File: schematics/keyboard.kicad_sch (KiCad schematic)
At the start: 33 parts, among them J2 Mini-DIN-6, Q1 2N7000, Q2 2N7000, Q3 2N7000, Q4 2N7000, U18 74HC14, U19 74HC04, U20 74HC00, U21 ATF22V10C-7, U22 74HC280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

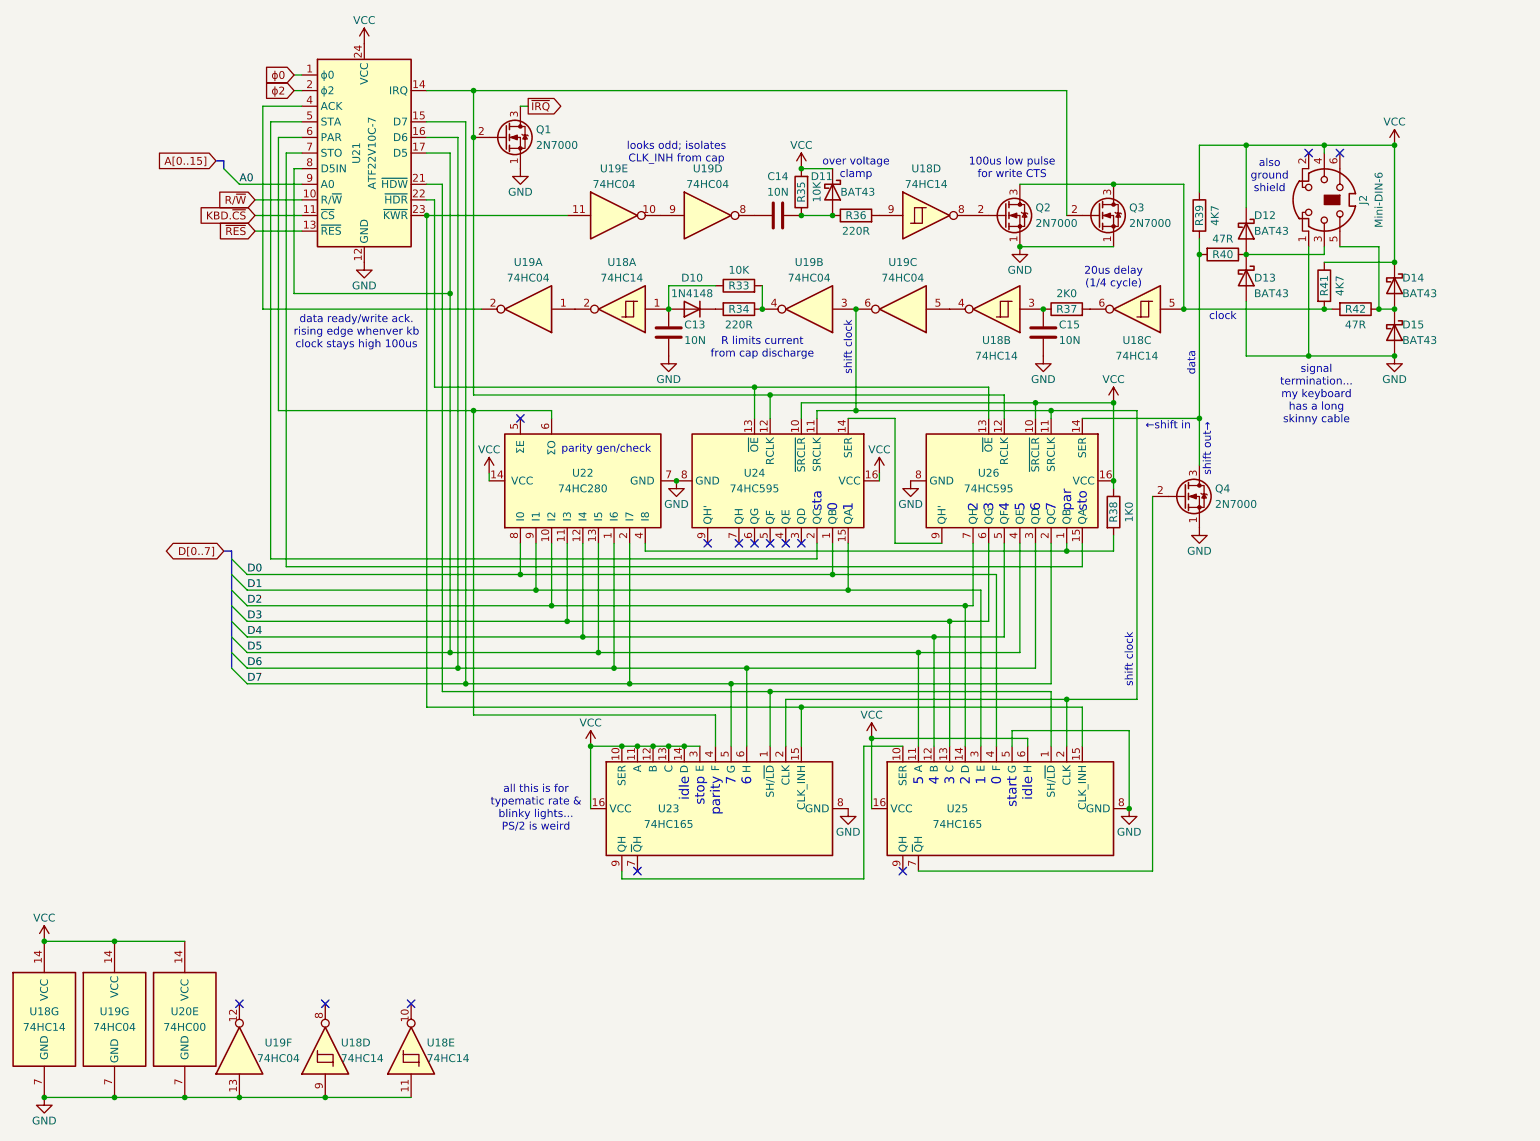
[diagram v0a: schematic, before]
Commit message: combined reset inputs in the pld
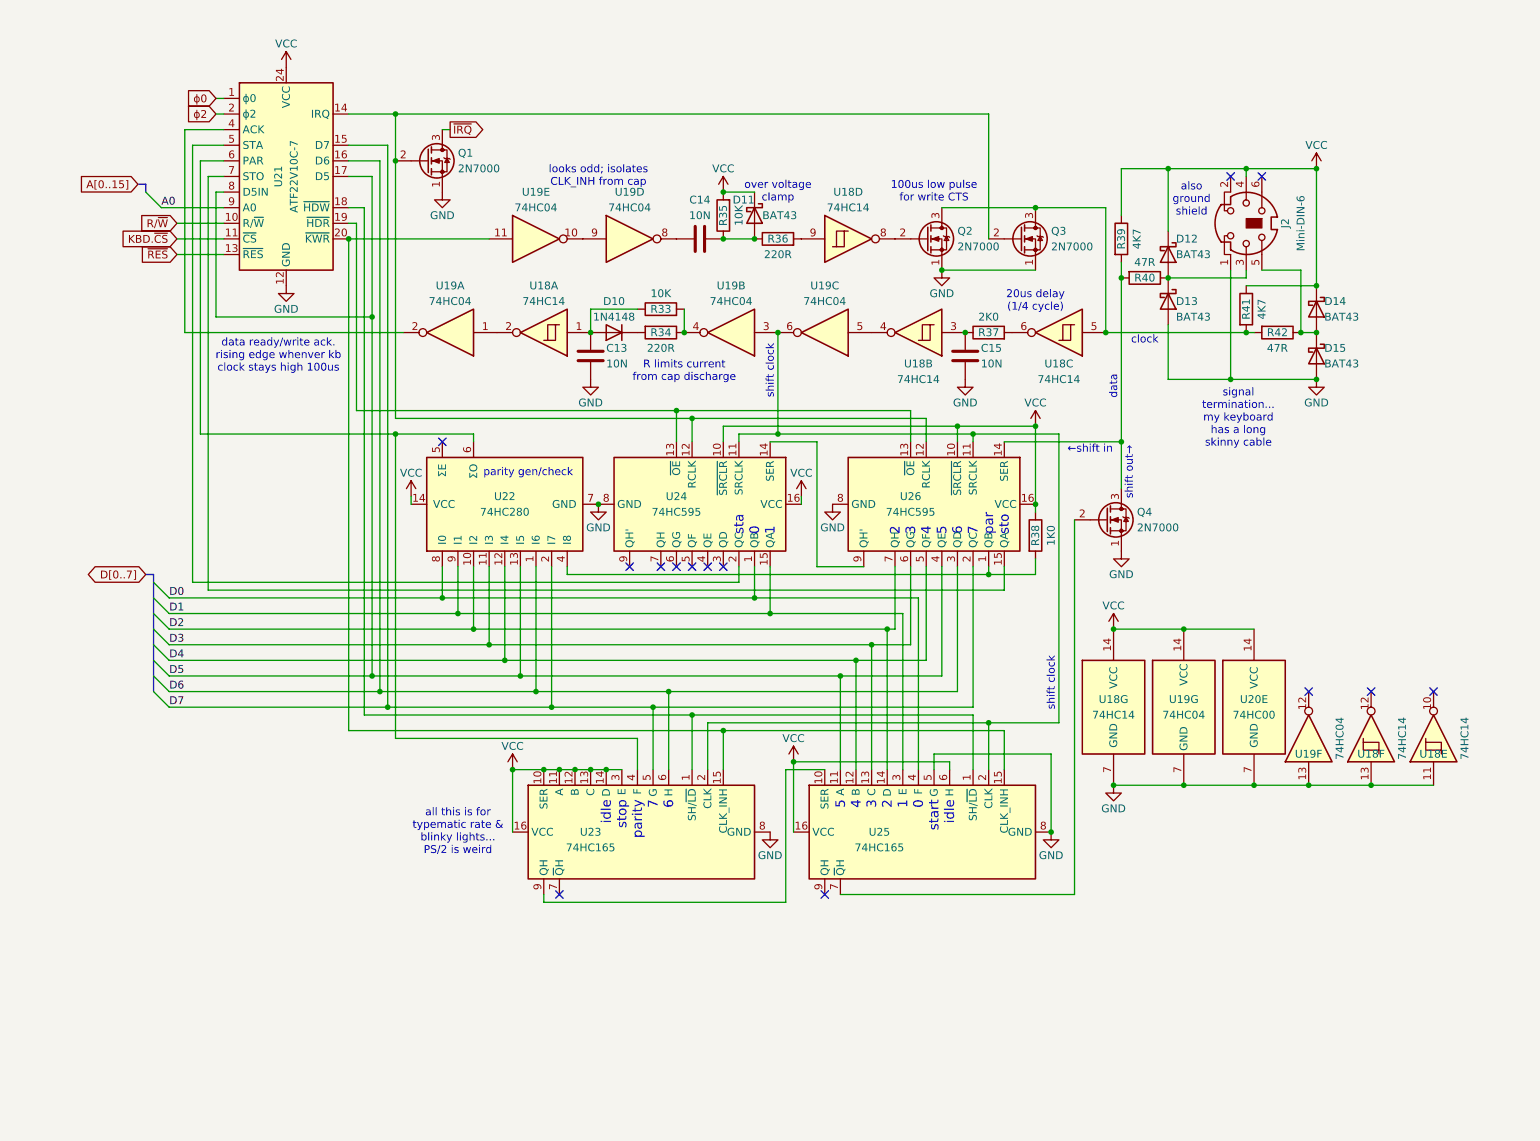
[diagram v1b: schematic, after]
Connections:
- net GND: now also U18.13; no longer U18.9
- net at U24.13 (~{OE}), U26.13 (~{OE}): now also U21.19 (~{HDR}); no longer U21.22 (~{HDR})
- net at U21.18 (~{HDW}): now also U23.1 (SH/~{LD}), U25.1 (SH/~{LD})
- net at U21.20 (~{KWR}): now also U19.11, U23.15 (CLK_INH), U25.15 (CLK_INH)
- now unconnected: U21.21 (~{HDW}), U21.23 (~{KWR})
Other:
- moved on the sheet: C13, C14, C15, D10, D11, D12, D13, D14, D15, J2, Q1, Q2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

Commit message: removed the 74hc04 from the keyboard
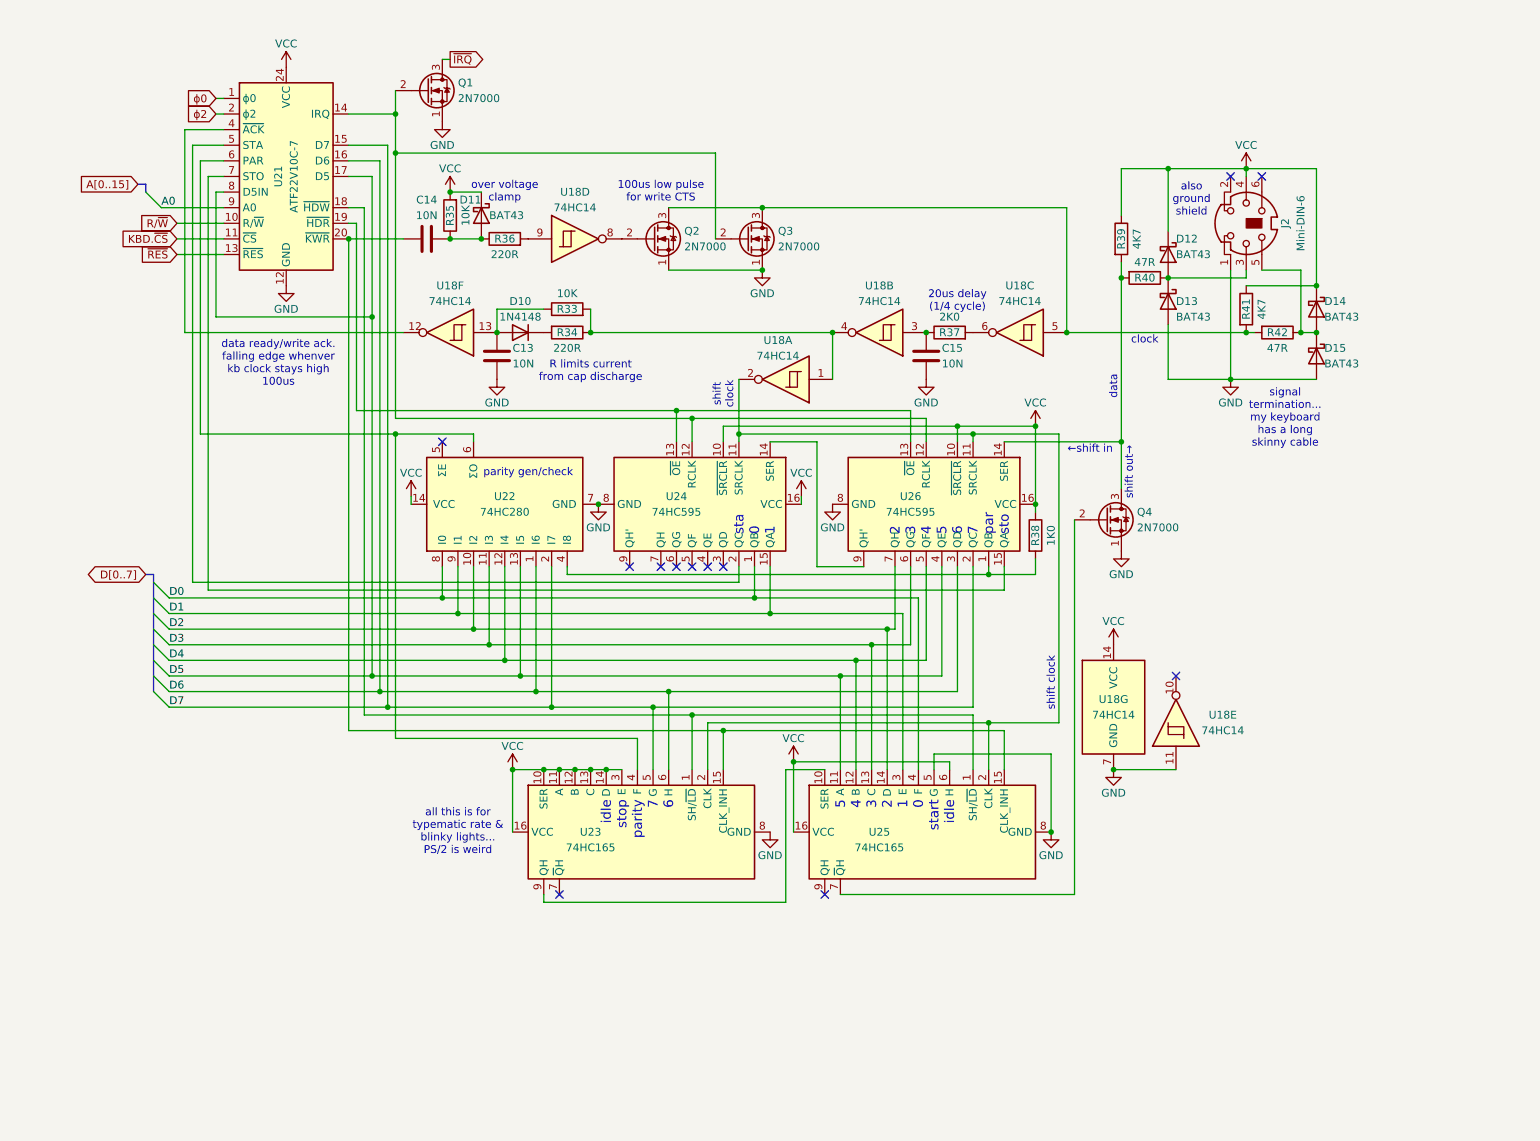
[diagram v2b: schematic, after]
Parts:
- removed unit 6 of U18
- removed U19: 74HC04, symbol 74xx:74HC04
- removed U20: 74HC00, symbol 74xx:74HC00
- added unit 1 of U18
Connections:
- net at U23.2 (CLK), U24.11 (SRCLK), U25.2 (CLK)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: now also U18.2
- net at U21.20 (~{KWR}), U23.15 (CLK_INH), U25.15 (CLK_INH): now also C14.1
- net at U21.4 (~{ACK}): now also U18.12
- net at C13.1, D10.2 (A), R33.1: now also U18.13; no longer U18.1
- net at U18.4: now also R33.2, R34.1, U18.1
- no-connect marks 14 -> 12
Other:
- note added: "data ready/write ack. falling edge whenver kb clock stays high 100us"
- note removed: "data ready/write ack. rising edge whenver kb clock stays high 100us"
- note removed: "looks odd; isolates CLK_INH from cap"
- moved on the sheet: C13, C14, C15, D10, D11, Q1, Q2, Q3, R33, R34, R35, R36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

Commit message: re-added the 74hc04 to the keyboard
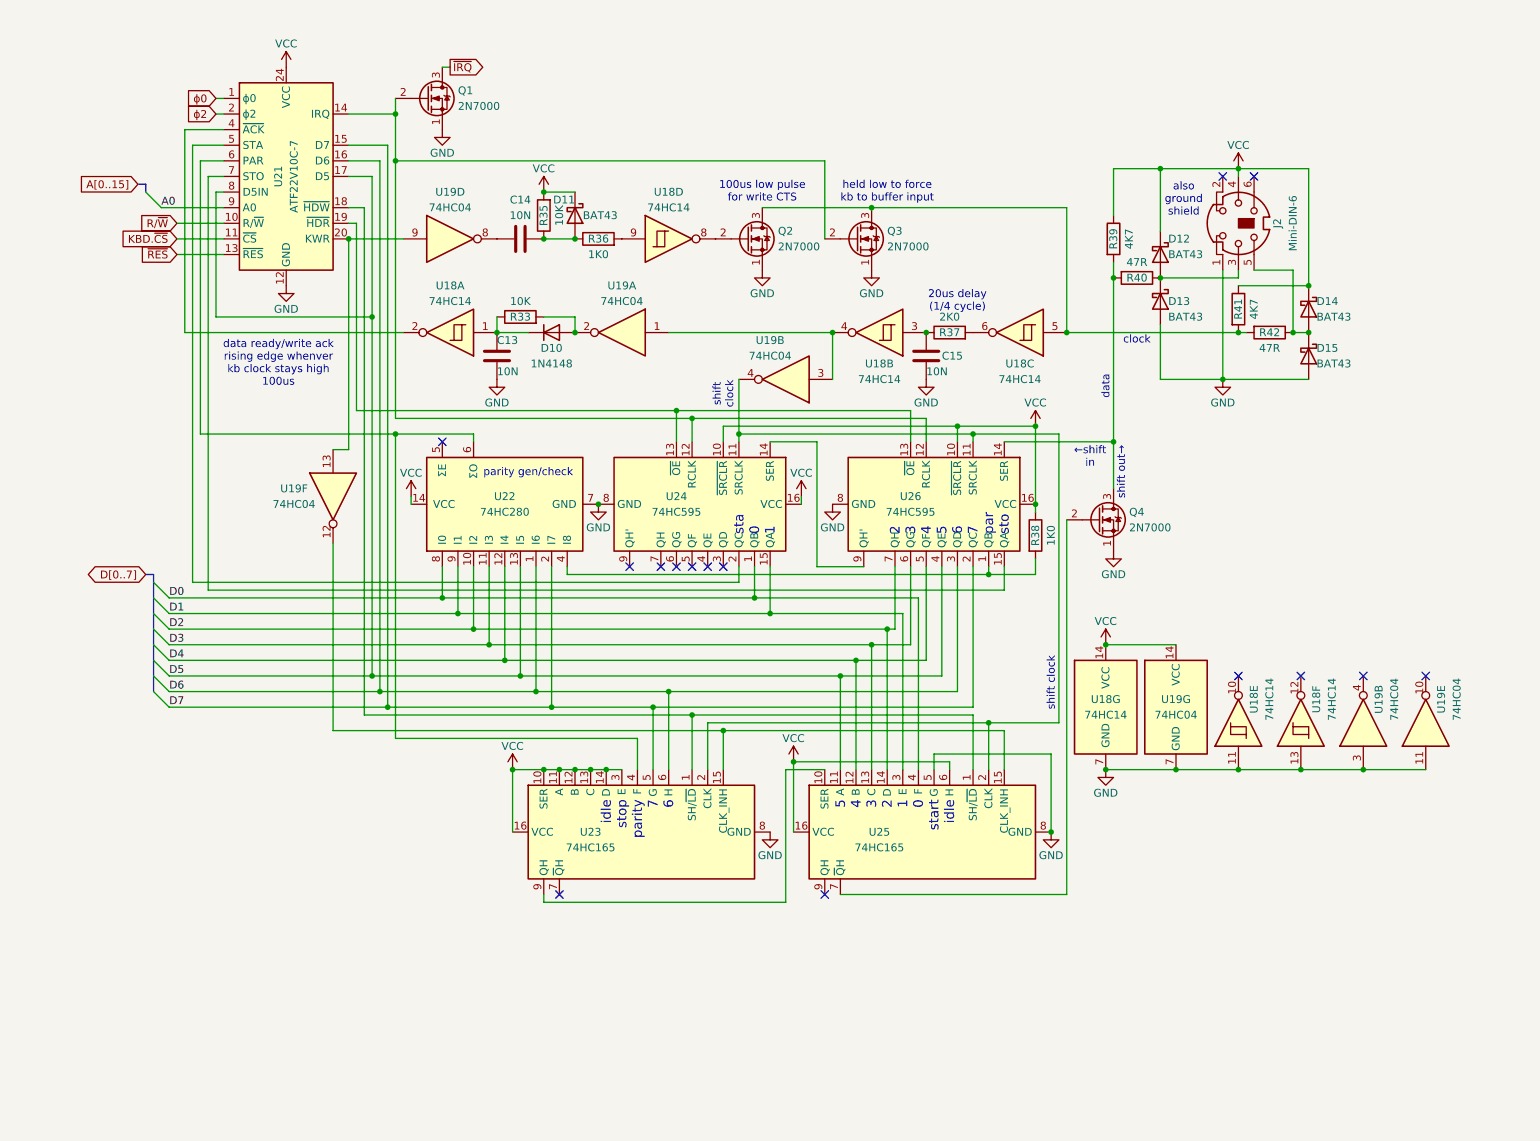
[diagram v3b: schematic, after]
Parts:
- removed R34: 220R, symbol Device:R
- removed unit 1 of U18
- added unit 6 of U18
- added U19: 74HC04, symbol 74xx:74HC04
- R36: value 220R -> 1K0
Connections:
- net GND: now also U18.13, U19.11, U19.3, U19.7 (GND)
- net VCC: now also U19.14 (VCC)
- net at U23.2 (CLK), U24.11 (SRCLK), U25.2 (CLK)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: now also U19.4
- net at U23.15 (CLK_INH), U25.15 (CLK_INH): now also U19.12; no longer C14.1, U21.20 (~{KWR})
- net at U21.4 (~{ACK}): now also U18.2; no longer U18.12
- net at D10.1 (K): now also C13.1, R33.1, U18.1
- net at U18.4: now also U19.1, U19.3; no longer R33.2
- new net: D10.2 (A), R33.2, U19.2
- new net: C14.1, U19.8
- new net: U19.13, U19.9, U21.20 (KWR)
- no-connect marks 12 -> 15
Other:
- note added: "data ready/write ack rising edge whenver kb clock stays high 100us"
- note added: "held low to force kb to buffer input"
- note removed: "R limits current from cap discharge"
- note removed: "all this is for typematic rate & blinky lights... PS/2 is weird"
- note removed: "data ready/write ack. falling edge whenver kb clock stays high 100us"
- note removed: "over voltage clamp"
- note removed: "signal termination... my keyboard has a long skinny cable"
- moved on the sheet: C14, D10, D11, D12, D13, D14, D15, J2, Q1, Q2, Q3, Q4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

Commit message: my keyboard needed a transceiver after all :(
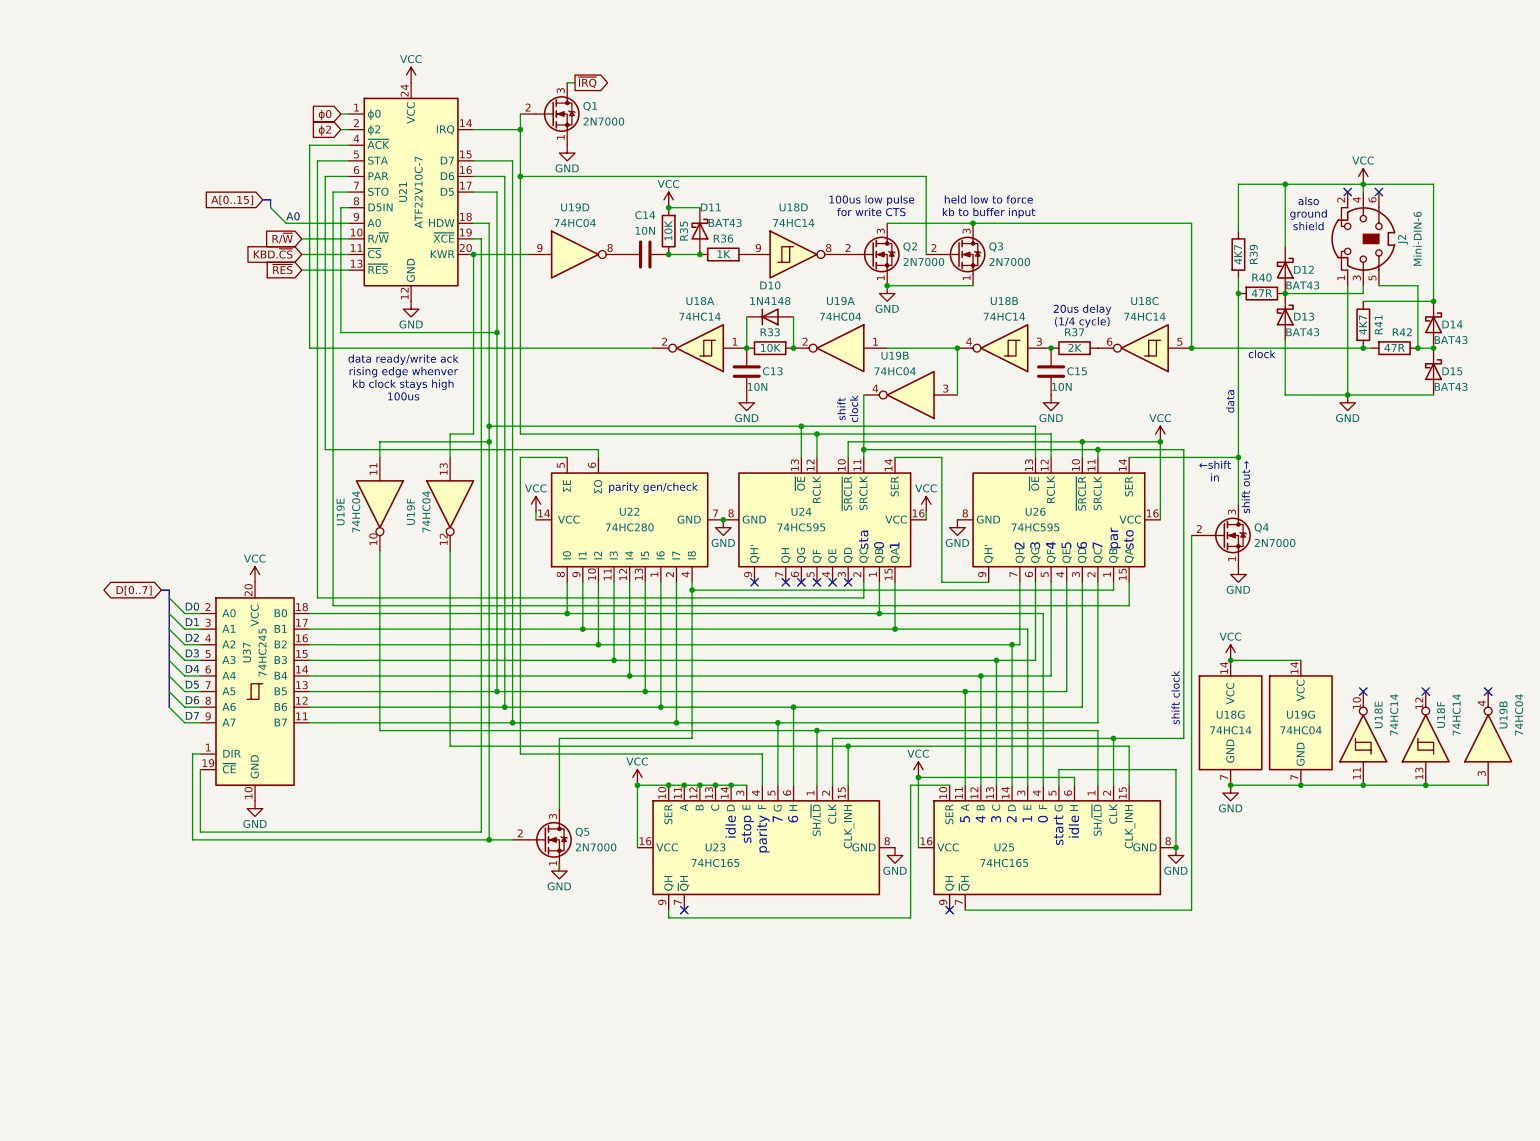
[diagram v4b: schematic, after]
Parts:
- removed R38: 1K0, symbol Device:R
- added Q5: 2N7000, Package_TO_SOT_THT:TO-92_Inline, symbol Transistor_FET:2N7000
- added U37: 74HC245, symbol 74xx:74HC245
- R36: value 1K0 -> 1K
- R37: value 2K0 -> 2K
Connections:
- net D0: now also U37.2 (A0); no longer U22.8 (I0), U24.1 (QB), U25.4 (F)
- net D1: now also U37.3 (A1); no longer U22.9 (I1), U24.15 (QA), U25.3 (E)
- net D2: now also U37.4 (A2); no longer U22.10 (I2), U25.14 (D), U26.7 (QH)
- net D3: now also U37.5 (A3); no longer U22.11 (I3), U25.13 (C), U26.6 (QG)
- net D4: now also U37.6 (A4); no longer U22.12 (I4), U25.12 (B), U26.5 (QF)
- net D5: now also U37.7 (A5); no longer U21.17 (D5), U21.8 (D5IN), U22.13 (I5), U25.11 (A), U26.4 (QE)
- net D6: now also U37.8 (A6); no longer U21.16 (D6), U22.1 (I6), U23.6 (H), U26.3 (QD)
- net D7: now also U37.9 (A7); no longer U21.15 (D7), U22.2 (I7), U23.5 (G), U26.2 (QC)
- net GND: now also Q5.1 (S), U37.10 (GND); no longer U19.11
- net VCC: now also U37.20 (VCC)
- net at U24.13 (~{OE}), U26.13 (~{OE}): now also U19.11, U21.18 (HDW), Q5.2 (G), U37.1 (DIR); no longer U21.19 (~{HDR})
- net at U19.10: now also U23.1 (SH/~{LD}), U25.1 (SH/~{LD})
- net at U21.6 (PAR), U22.6 (ΣO): no longer U23.4 (F)
- net at U22.4 (I8), U26.1 (QB): now also Q5.3 (D)
- net at U22.5 (ΣE): now also U23.4 (F)
- new net: U22.8 (I0), U24.1 (QB), U25.4 (F), U37.18 (B0)
- new net: U22.9 (I1), U24.15 (QA), U25.3 (E), U37.17 (B1)
- new net: U21.15 (D7), U22.2 (I7), U23.5 (G), U26.2 (QC), U37.11 (B7)
- new net: U21.16 (D6), U22.1 (I6), U23.6 (H), U26.3 (QD), U37.12 (B6)
- new net: U21.17 (D5), U21.8 (D5IN), U22.13 (I5), U25.11 (A), U26.4 (QE), U37.13 (B5)
- new net: U21.19 (~{XCE}), U37.19 (~{CE})
- new net: U22.10 (I2), U25.14 (D), U26.7 (QH), U37.16 (B2)
- new net: U22.11 (I3), U25.13 (C), U26.6 (QG), U37.15 (B3)
- new net: U22.12 (I4), U25.12 (B), U26.5 (QF), U37.14 (B4)
- no-connect marks 15 -> 13
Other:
- moved on the sheet: C13, C14, C15, D10, D11, D12, D13, D14, D15, J2, Q1, Q2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
